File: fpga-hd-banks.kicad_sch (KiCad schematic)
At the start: 16 parts, among them Q4 BSS138PW, Q5 BSS138PW, Q6 BSS138PW, Q7 BSS138PW, Q8 BSS138PW, U34 XCAU25P-2FFVB676I

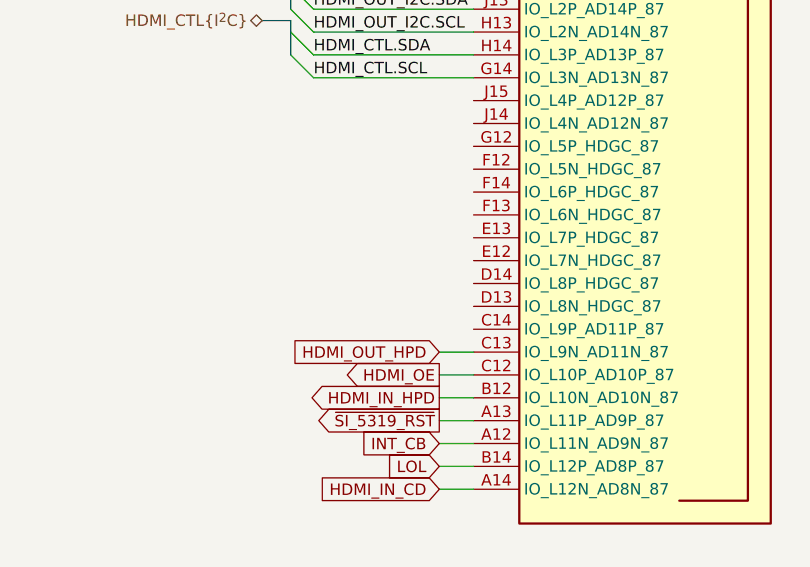
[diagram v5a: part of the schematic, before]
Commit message: [#66727] Minor schematic improvements. Finish routing right side of the board
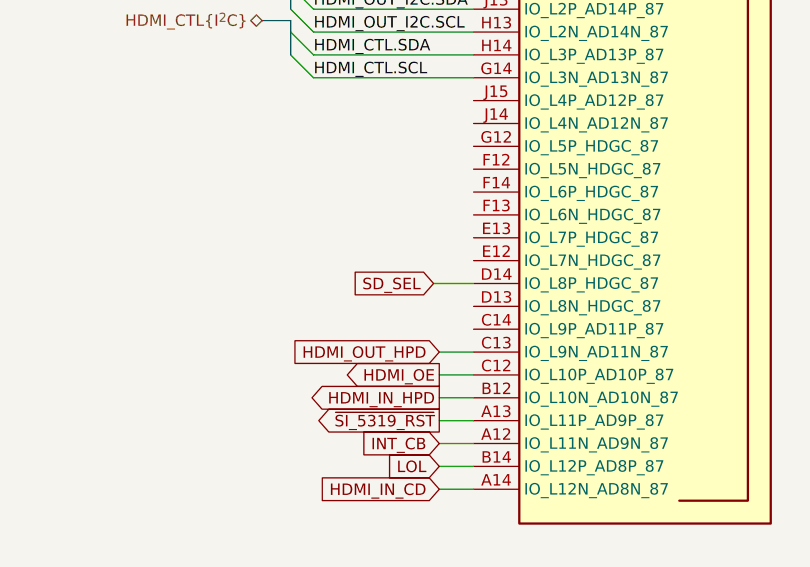
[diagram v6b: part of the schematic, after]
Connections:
- net SD_SEL: now reaches U34.D14 (IO_L8P_HDGC_87)
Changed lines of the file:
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@@
+    (stroke (width 0) (type default))
+  )
+  (wire (pts (xy 207.645 151.13) (xy 212.09 151.13))
     (stroke (width 0) (type default))
   )
@@
       (effects (font (size 1.27 1.27)) (justify right))
     )
+  )
+  (global_label "SD_SEL" (shape input) (at 207.645 151.13 180) (fields_autoplaced)
+    (effects (font (size 1.27 1.27)) (justify right))
+    (property "Intersheetrefs" "${INTERSHEET_REFS}" (at 197.8261 151.13 0)
+      (effects (font (size 1.27 1.27)) (justify right))
+    )

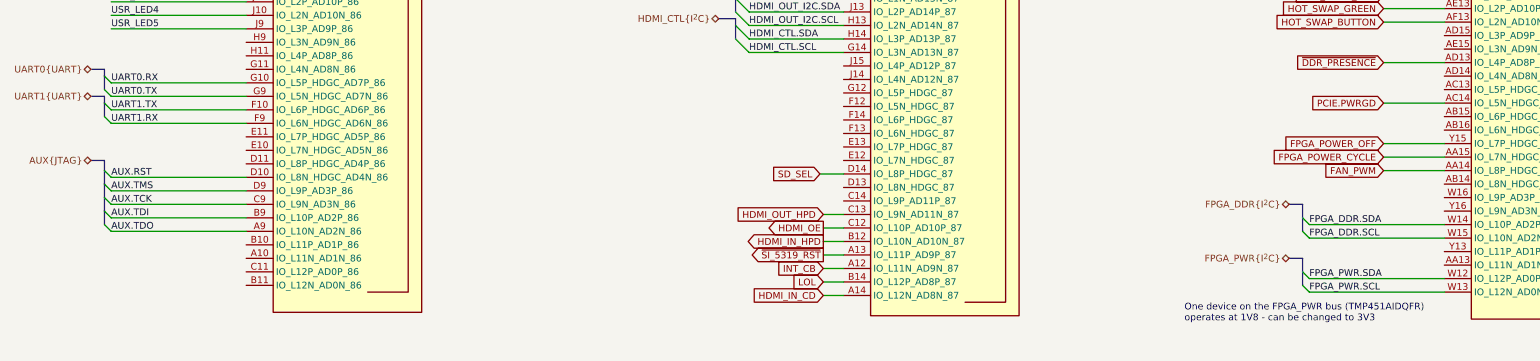
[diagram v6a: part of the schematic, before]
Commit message: [#67532] Finalize routing
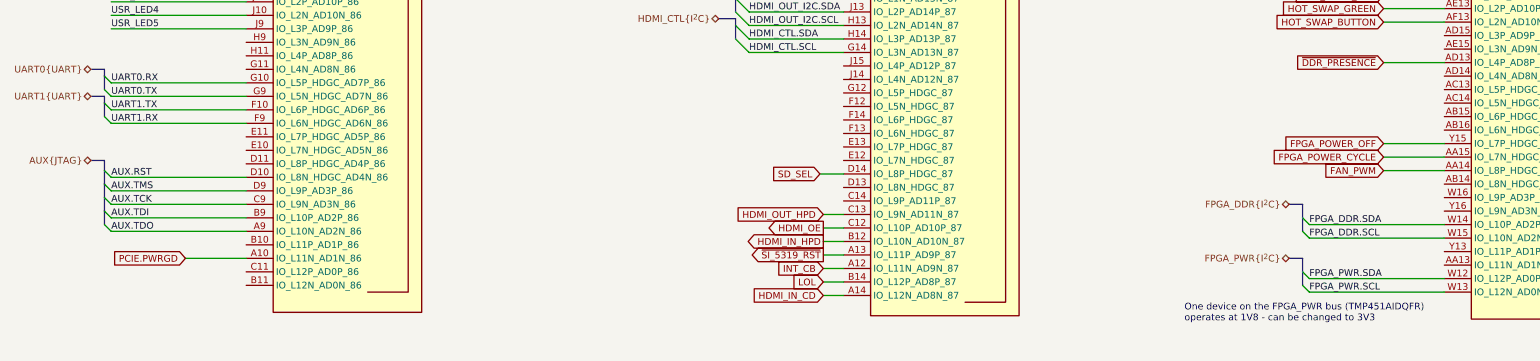
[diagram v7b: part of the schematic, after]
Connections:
- net PCIE.PWRGD: now also U34.A10 (IO_L11N_AD1N_86); no longer U34.AC14 (IO_L5N_HDGC_AD7N_84)
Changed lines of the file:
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@@
     (stroke (width 0) (type default))
   )
-  (wire (pts (xy 313.69 137.795) (xy 325.12 137.795))
+  (wire (pts (xy 88.265 167.005) (xy 99.695 167.005))
     (stroke (width 0) (type default))
   )
@@
     )
   )
-  (global_label "PCIE.PWRGD" (shape input) (at 313.69 137.795 180) (fields_autoplaced)
-    (effects (font (size 1.27 1.27)) (justify right))
-    (property "Intersheetrefs" "${INTERSHEET_REFS}" (at 299.9358 137.8744 0)
-      (effects (font (size 1.27 1.27)) (justify right))
-    )
+  (global_label "PCIE.PWRGD" (shape input) (at 88.265 167.005 180) (fields_autoplaced)
+    (effects (font (size 1.27 1.27)) (justify right))
+    (property "Intersheetrefs" "${INTERSHEET_REFS}" (at 74.5108 167.0844 0)
+      (effects (font (size 1.27 1.27)) (justify right))
+    )

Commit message: [#67725] Connect I3C signals to the FPGA
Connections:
- net FPGA_I3C.SCL: now reaches U34.F12 (IO_L5N_HDGC_87)
- net ~{FPGA_I3C_EXT_PU}: now reaches U34.F13 (IO_L6N_HDGC_87)
- net ~{I3C_EXT_PU}: now reaches U34.F14 (IO_L6P_HDGC_87)
- net FPGA_I3C.SDA: now reaches U34.G12 (IO_L5P_HDGC_87)
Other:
- note removed: "Left FPGA side"
- note removed: "One device on the FPGA_PWR bus (TMP451AIDQFR) operates at 1V8 - can be changed to 3V3"
- note removed: "Right FPGA side"
- moved on the sheet: D4, D5, D6, D7, D8, Q4, Q5, Q6, Q7, Q8, R40, R41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
